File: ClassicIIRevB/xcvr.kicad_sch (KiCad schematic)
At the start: 2 parts, among them U20 74LS245, U21 74LS245

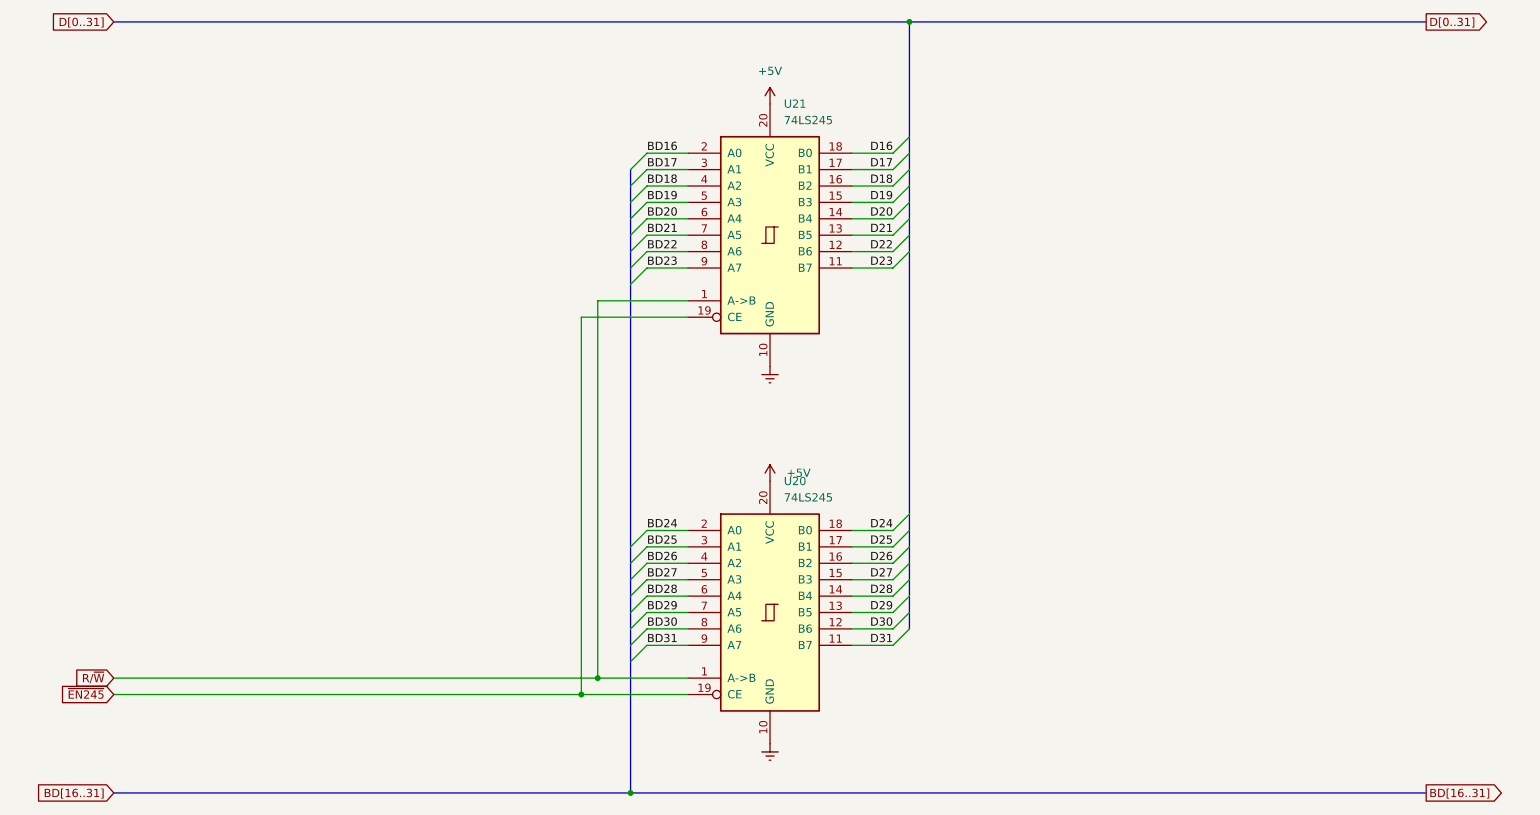
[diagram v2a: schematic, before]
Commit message: Switch to some "official" net names
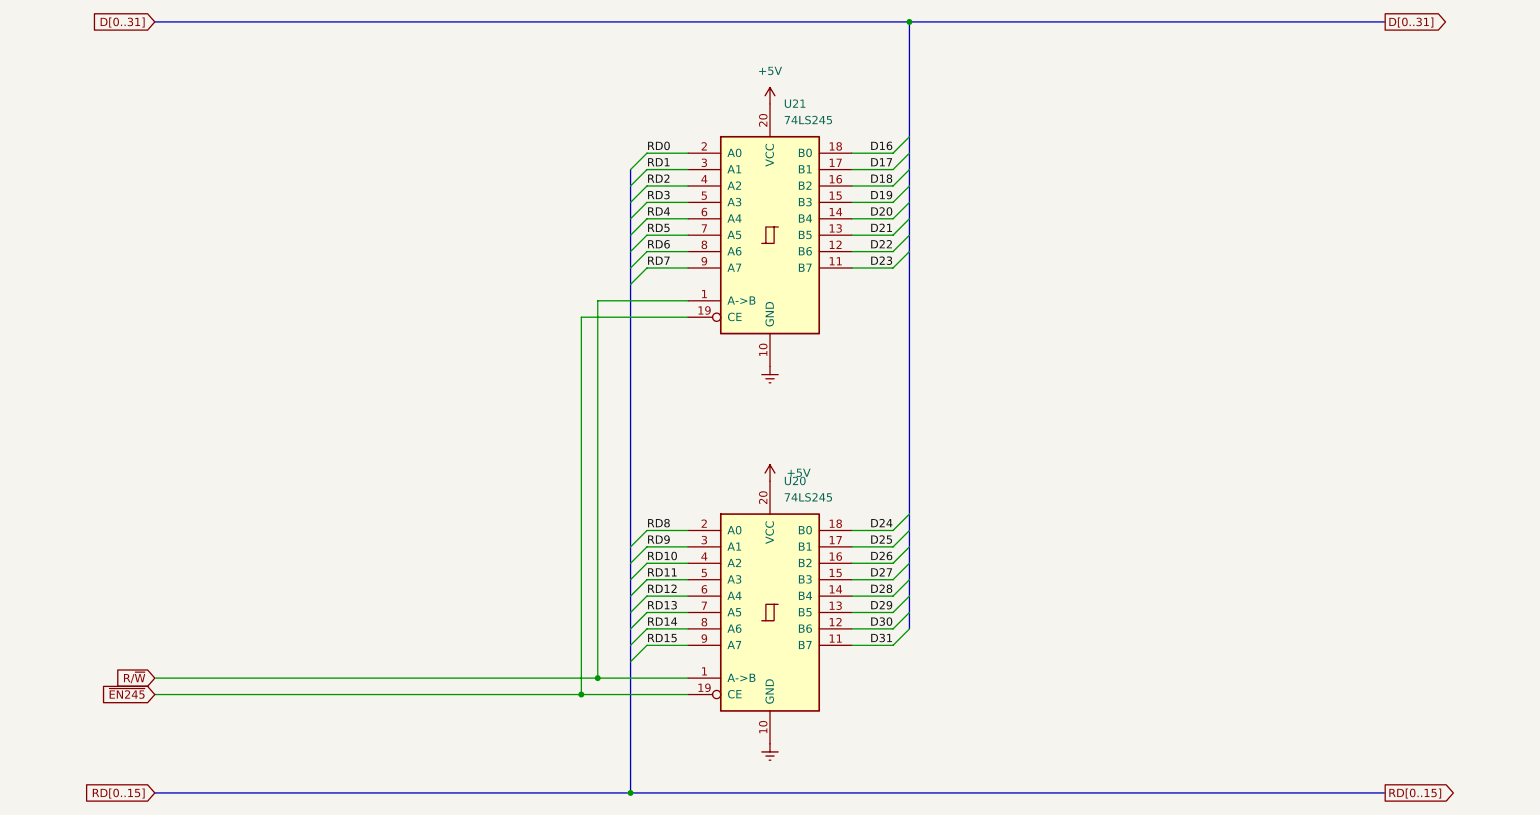
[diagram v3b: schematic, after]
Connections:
- net BD16 renamed RD0
- net BD17 renamed RD1
- net BD18 renamed RD2
- net BD19 renamed RD3
- net BD20 renamed RD4
- net BD21 renamed RD5
- net BD22 renamed RD6
- net BD23 renamed RD7
- net BD24 renamed RD8
- net BD25 renamed RD9
- net BD26 renamed RD10
- net BD27 renamed RD11
- net BD28 renamed RD12
- net BD29 renamed RD13
- net BD30 renamed RD14
- net BD31 renamed RD15
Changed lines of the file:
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@@
 	(wire
 		(pts
-			(xy 113.03 139.7) (xy 38.1 139.7)
+			(xy 113.03 139.7) (xy 44.45 139.7)
 		)
 		(stroke
@@
 	(wire
 		(pts
-			(xy 38.1 142.24) (xy 110.49 142.24)
+			(xy 44.45 142.24) (xy 110.49 142.24)
 		)
 		(stroke
@@
 	(bus
 		(pts
-			(xy 38.1 38.1) (xy 161.29 38.1)
+			(xy 44.45 38.1) (xy 161.29 38.1)
 		)
 		(stroke
@@
 	(bus
 		(pts
-			(xy 118.11 157.48) (xy 241.3 157.48)
+			(xy 118.11 157.48) (xy 234.95 157.48)
 		)
 		(stroke
@@
 	(bus
 		(pts
-			(xy 161.29 38.1) (xy 241.3 38.1)
-		)
-		(stroke
-			(width 0)
-			(type default)
-		)
-	)
-	(bus
-		(pts
-			(xy 38.1 157.48) (xy 118.11 157.48)
+			(xy 161.29 38.1) (xy 234.95 38.1)
+		)
+		(stroke
+			(width 0)
+			(type default)
+		)
+	)
+	(bus
+		(pts
+			(xy 44.45 157.48) (xy 118.11 157.48)
 		)
 		(stroke
@@
 			(width 0)
 			(type default)
+		)
+	)
+	(label "RD13"
+		(at 120.65 129.54 0)
+		(effects
+			(font
+				(size 1.27 1.27)
+			)
+			(justify left bottom)
+		)
+	)
+	(label "RD0"
+		(at 120.65 58.42 0)
+		(effects
+			(font
+				(size 1.27 1.27)
+			)
+			(justify left bottom)
 		)
 	)
@@
 		)
 	)
+	(label "RD10"
+		(at 120.65 121.92 0)
+		(effects
+			(font
+				(size 1.27 1.27)
+			)
+			(justify left bottom)
+		)
+	)
 	(label "D21"
 		(at 158.75 71.12 180)
@@
 		)
 	)
-	(label "BD18"
-		(at 120.65 63.5 0)
-		(effects
-			(font
-				(size 1.27 1.27)
-			)
-			(justify left bottom)
-		)
-	)
 	(label "D19"
 		(at 158.75 66.04 180)
@@
 		)
 	)
-	(label "BD19"
-		(at 120.65 66.04 0)
-		(effects
-			(font
-				(size 1.27 1.27)
-			)
-			(justify left bottom)
-		)
-	)
 	(label "D22"
 		(at 158.75 73.66 180)
@@
 		)
 	)
-	(label "BD21"
-		(at 120.65 71.12 0)
-		(effects
-			(font
-				(size 1.27 1.27)
-			)
-			(justify left bottom)
-		)
-	)
-	(label "BD24"
-		(at 120.65 116.84 0)
+	(label "RD2"
+		(at 120.65 63.5 0)
+		(effects
+			(font
+				(size 1.27 1.27)
+			)
+			(justify left bottom)
+		)
+	)
+	(label "RD15"
+		(at 120.65 134.62 0)
 		(effects
 			(font
@@
 		)
 	)
-	(label "BD29"
-		(at 120.65 129.54 0)
-		(effects
-			(font
-				(size 1.27 1.27)
-			)
-			(justify left bottom)
-		)
-	)
-	(label "BD25"
+	(label "RD9"
 		(at 120.65 119.38 0)
-		(effects
-			(font
-				(size 1.27 1.27)
-			)
-			(justify left bottom)
-		)
-	)
-	(label "BD31"
-		(at 120.65 134.62 0)
 		(effects
 			(font
@@
 		)
 	)
-	(label "BD27"
-		(at 120.65 124.46 0)
-		(effects
-			(font
-				(size 1.27 1.27)
-			)
-			(justify left bottom)
-		)
-	)
 	(label "D24"
 		(at 158.75 116.84 180)
@@
 		)
 	)
-	(label "BD17"
-		(at 120.65 60.96 0)
-		(effects
-			(font
-				(size 1.27 1.27)
-			)
-			(justify left bottom)
-		)
-	)
-	(label "BD30"
-		(at 120.65 132.08 0)
+	(label "RD6"
+		(at 120.65 73.66 0)
 		(effects
 			(font
@@
 		)
 	)
-	(label "BD20"
-		(at 120.65 68.58 0)
+	(label "RD7"
+		(at 120.65 76.2 0)
 		(effects
 			(font
@@
 		)
 	)
-	(label "BD26"
-		(at 120.65 121.92 0)
+	(label "RD4"
+		(at 120.65 68.58 0)
+		(effects
+			(font
+				(size 1.27 1.27)
+			)
+			(justify left bottom)
+		)
+	)
+	(label "RD12"
+		(at 120.65 127 0)
 		(effects
 			(font
@@
 		)
 	)
+	(label "RD1"
+		(at 120.65 60.96 0)
+		(effects
+			(font
+				(size 1.27 1.27)
+			)
+			(justify left bottom)
+		)
+	)
+	(label "RD5"
+		(at 120.65 71.12 0)
+		(effects
+			(font
+				(size 1.27 1.27)
+			)
+			(justify left bottom)
+		)
+	)
+	(label "RD11"
+		(at 120.65 124.46 0)
+		(effects
+			(font
+				(size 1.27 1.27)
+			)
+			(justify left bottom)
+		)
+	)
 	(label "D31"
 		(at 158.75 134.62 180)
@@
 		)
 	)
+	(label "RD14"
+		(at 120.65 132.08 0)
+		(effects
+			(font
+				(size 1.27 1.27)
+			)
+			(justify left bottom)
+		)
+	)
 	(label "D17"
 		(at 158.75 60.96 180)
@@
 		)
 	)
-	(label "BD28"
-		(at 120.65 127 0)
-		(effects
-			(font
-				(size 1.27 1.27)
-			)
-			(justify left bottom)
-		)
-	)
 	(label "D30"
 		(at 158.75 132.08 180)
@@
 		)
 	)
-	(label "BD22"
-		(at 120.65 73.66 0)
-		(effects
-			(font
-				(size 1.27 1.27)
-			)
-			(justify left bottom)
-		)
-	)
-	(label "BD23"
-		(at 120.65 76.2 0)
-		(effects
-			(font
-				(size 1.27 1.27)
-			)
-			(justify left bottom)
-		)
-	)
-	(label "BD16"
-		(at 120.65 58.42 0)
+	(label "RD3"
+		(at 120.65 66.04 0)
 		(effects
 			(font
@@
 		)
 	)
-	(global_label "BD[16..31]"
+	(label "RD8"
+		(at 120.65 116.84 0)
+		(effects
+			(font
+				(size 1.27 1.27)
+			)
+			(justify left bottom)
+		)
+	)
+	(global_label "RD[0..15]"
 		(shape output)
-		(at 241.3 157.48 0)
+		(at 234.95 157.48 0)
 		(fields_autoplaced yes)
 		(effects
@@
 		)
 		(property "Intersheetrefs" "${INTERSHEET_REFS}"
-			(at 254.5662 157.48 0)
+			(at 248.2162 157.48 0)
 			(effects
 				(font
@@
 	(global_label "~{EN245}"
 		(shape input)
-		(at 38.1 142.24 180)
+		(at 44.45 142.24 180)
 		(fields_autoplaced yes)
 		(effects
@@
 		)
 		(property "Intersheetrefs" "${INTERSHEET_REFS}"
-			(at 28.8253 142.24 0)
+			(at 35.1753 142.24 0)
 			(effects
 				(font
@@
 	(global_label "D[0..31]"
 		(shape output)
-		(at 241.3 38.1 0)
+		(at 234.95 38.1 0)
 		(fields_autoplaced yes)
 		(effects
@@
 		)
 		(property "Intersheetrefs" "${INTERSHEET_REFS}"
-			(at 252.0867 38.1 0)
+			(at 245.7367 38.1 0)
 			(effects
 				(font
@@
 	(global_label "R{slash}~{W}"
 		(shape input)
-		(at 38.1 139.7 180)
+		(at 44.45 139.7 180)
 		(fields_autoplaced yes)
 		(effects
@@
 		)
 		(property "Intersheetrefs" "${INTERSHEET_REFS}"
-			(at 31.0629 139.7 0)
+			(at 37.4129 139.7 0)
 			(effects
 				(font
@@
 		)
 	)
-	(global_label "BD[16..31]"
+	(global_label "RD[0..15]"
 		(shape input)
-		(at 38.1 157.48 180)
+		(at 44.45 157.48 180)
 		(fields_autoplaced yes)
 		(effects
@@
 		)
 		(property "Intersheetrefs" "${INTERSHEET_REFS}"
-			(at 24.8338 157.48 0)
+			(at 32.3933 157.48 0)
 			(effects
 				(font
@@
 	(global_label "D[0..31]"
 		(shape input)
-		(at 38.1 38.1 180)
+		(at 44.45 38.1 180)
 		(fields_autoplaced yes)
 		(effects
@@
 		)
 		(property "Intersheetrefs" "${INTERSHEET_REFS}"
-			(at 27.3133 38.1 0)
+			(at 33.6633 38.1 0)
 			(effects
 				(font

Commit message: update exports
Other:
- title: Macintosh Classic II Revision B -> Macintosh Classic II (Later Revision)
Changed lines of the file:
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@@
 	(paper "USLetter")
 	(title_block
-		(title "Macintosh Classic II Revision B")
-		(date "2025-06-04")
+		(title "Macintosh Classic II (Later Revision)")
+		(date "2025-06-16")
 		(company "Apple Computer")
 		(comment 1 "drawn by Bradley Bell")

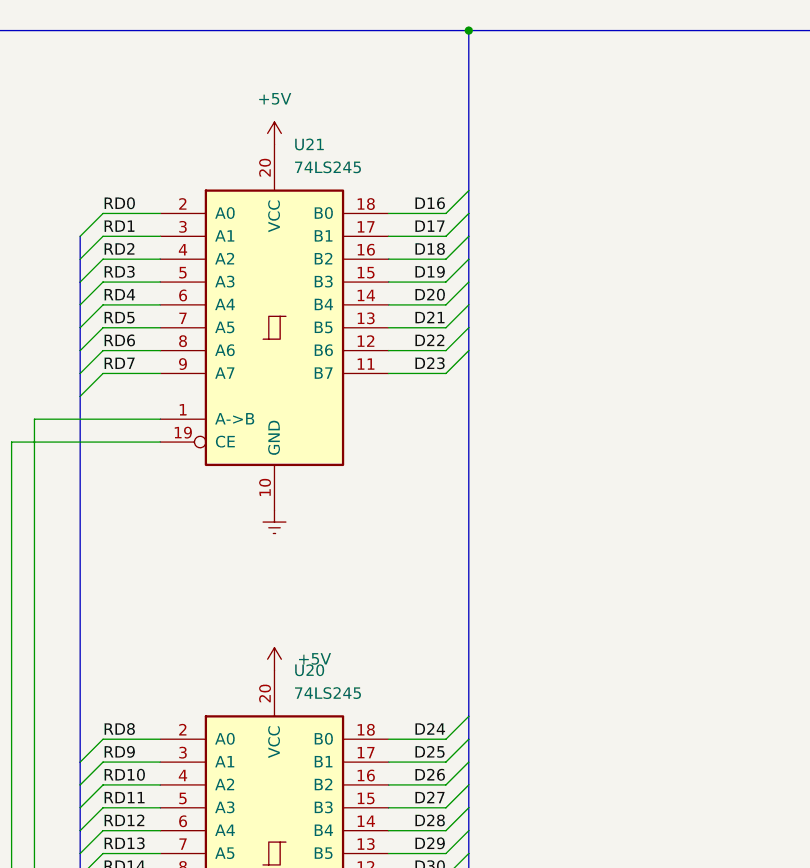
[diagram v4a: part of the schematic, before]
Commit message: Corrections to SMDs, more improved footprints
The later revision board reproduction design is now complete.
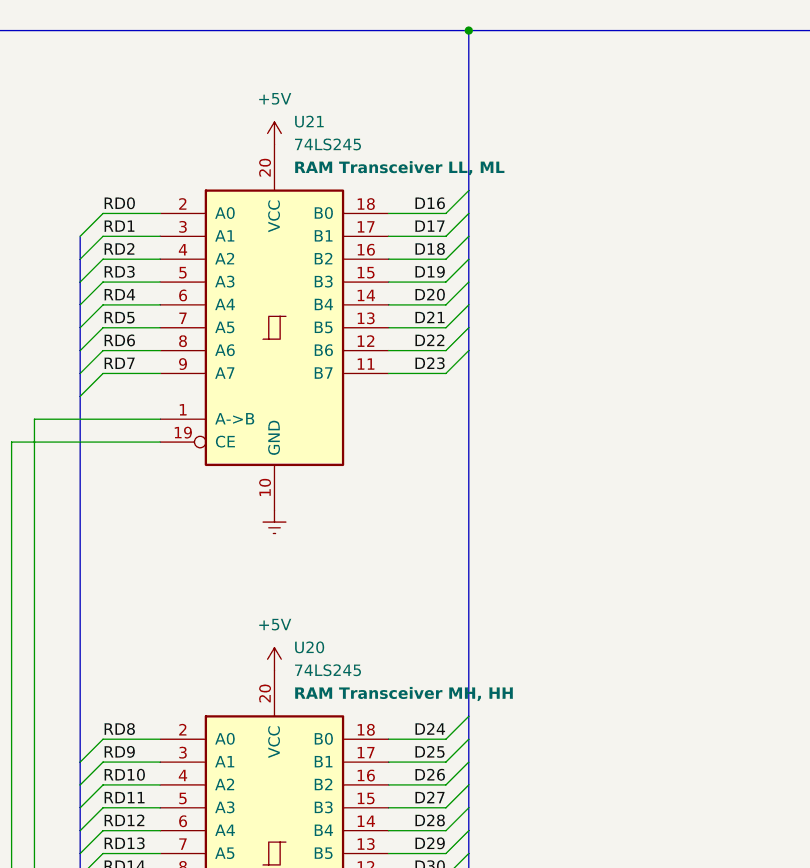
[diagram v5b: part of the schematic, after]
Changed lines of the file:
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@@
 	(title_block
 		(title "Macintosh Classic II (Later Revision)")
-		(date "2025-06-16")
+		(date "2025-06-21")
 		(company "Apple Computer")
 		(comment 1 "drawn by Bradley Bell")
@@
 		)
 		(property "Intersheetrefs" "${INTERSHEET_REFS}"
-			(at 248.2162 157.48 0)
+			(at 247.0067 157.48 0)
 			(effects
 				(font
@@
 		(fields_autoplaced yes)
 		(property "Reference" "U21"
+			(at 141.8433 48.26 0)
+			(effects
+				(font
+					(size 1.27 1.27)
+				)
+				(justify left)
+			)
+		)
+		(property "Value" "74LS245"
 			(at 141.8433 50.8 0)
-			(effects
-				(font
-					(size 1.27 1.27)
-				)
-				(justify left)
-			)
-		)
-		(property "Value" "74LS245"
-			(at 141.8433 53.34 0)
 			(effects
 				(font
@@
 			)
 		)
-		(property "Description" "Octal BUS Transceivers, 3-State outputs"
-			(at 139.7 71.12 0)
-			(effects
-				(font
-					(size 1.27 1.27)
-				)
-				(hide yes)
+		(property "Description" "RAM Transceiver LL, ML"
+			(at 141.8433 53.34 0)
+			(effects
+				(font
+					(size 1.27 1.27)
+					(thickness 0.254)
+					(bold yes)
+				)
+				(justify left)
 			)
 		)
@@
 		(fields_autoplaced yes)
 		(property "Reference" "U20"
+			(at 141.8433 106.68 0)
+			(effects
+				(font
+					(size 1.27 1.27)
+				)
+				(justify left)
+			)
+		)
+		(property "Value" "74LS245"
 			(at 141.8433 109.22 0)
-			(effects
-				(font
-					(size 1.27 1.27)
-				)
-				(justify left)
-			)
-		)
-		(property "Value" "74LS245"
-			(at 141.8433 111.76 0)
 			(effects
 				(font
@@
 			)
 		)
-		(property "Description" "Octal BUS Transceivers, 3-State outputs"
-			(at 139.7 129.54 0)
-			(effects
-				(font
-					(size 1.27 1.27)
-				)
-				(hide yes)
+		(property "Description" "RAM Transceiver MH, HH"
+			(at 141.8433 111.76 0)
+			(effects
+				(font
+					(size 1.27 1.27)
+					(thickness 0.254)
+					(bold yes)
+				)
+				(justify left)
 			)
 		)
@@
 		)
 		(property "Value" "+5V"
-			(at 142.24 107.9499 0)
-			(effects
-				(font
-					(size 1.27 1.27)
-				)
-				(justify right)
-			)
-		)
+			(at 139.7 104.14 0)
+			(effects
+				(font
+					(size 1.27 1.27)
+				)
+			)
+		)
